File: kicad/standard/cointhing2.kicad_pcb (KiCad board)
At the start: 2 copper layers, 35 x 34 mm, 29 parts, among them J1 USB_B_Micro, Q1 BC847BS, Q2 S8050_J3Y, U1 CP2102-GMR_NRND, U2 ESP-12E, U3 AMS1117-3.3

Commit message: Update cointhing2.kicad_pcb
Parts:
- added QR*****: https://github.com/barn53/CoinThing/tree/2inch, https://github.com/barn53/CoinThing/tree/2inch, B.Cu at (170.8, 63.0)
- moved R6 26.6 mm to (174.9, 78.7)
- moved R7 26.6 mm to (174.9, 77.2)
- moved R1 26.1 mm to (149.3, 85.3), turned to 180 degrees
- moved R2 24.7 mm to (152.3, 85.3), turned to 180 degrees
- moved R4 22.3 mm to (152.3, 86.8), turned to 180 degrees
- moved Q1 21.7 mm to (174.9, 81.3)
- moved C7 6.89 mm to (177.0, 68.1), turned to 0 degrees
- moved C6 6.70 mm to (174.0, 68.1), turned to 180 degrees
- moved R11 3.88 mm to (169.1, 85.3), turned to 0 degrees
- moved R9 3.88 mm to (169.1, 86.8)
- moved REF** 3.70 mm to (171.4, 72.2)
- moved C8 2.78 mm to (166.1, 86.8)
- moved R10 2.78 mm to (166.1, 85.3), turned to 180 degrees
- moved C9 2.27 mm to (170.0, 62.2), turned to 90 degrees
- moved C5 0.61 mm to (160.7, 86.8)
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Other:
- outline, holes or cut-outs redrawn

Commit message: finished PCB rev.A
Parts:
- QR*****: footprint https://github.com/barn53/CoinThing/tree/2inch -> https:__github.com_barn53_CoinThing_tree_2inch
- renumbered REF** to h1, REF** to h2
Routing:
- net +3V3: track 0.00 -> 94.6 mm, vias 0 -> 5
- net VBUS: track 0.00 -> 42.9 mm
- net /GPIO0: track 0.00 -> 41.8 mm, vias 0 -> 2
- net Net-(R4-Pad2): track 0.00 -> 36.4 mm
- net /DTR: track 0.00 -> 32.1 mm
- net /TFT_BL: track 0.00 -> 31.4 mm, vias 0 -> 2
- net /~TFT_RES: track 0.00 -> 30.7 mm, vias 0 -> 2
- net /RTS: track 0.00 -> 30.5 mm, vias 0 -> 2
- net /~Reset: track 0.00 -> 26.5 mm, vias 0 -> 2
- net /D-: track 0.00 -> 16.9 mm, vias 0 -> 2
- net /D+: track 0.00 -> 16.8 mm, vias 0 -> 2
- net /VDD: track 0.00 -> 16.7 mm, vias 0 -> 2
- net Net-(R3-Pad2): track 0.00 -> 16.0 mm
- net /TFT_SDA: track 0.00 -> 12.5 mm, vias 0 -> 1
- net Net-(Q2-Pad1): track 0.00 -> 10.6 mm
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
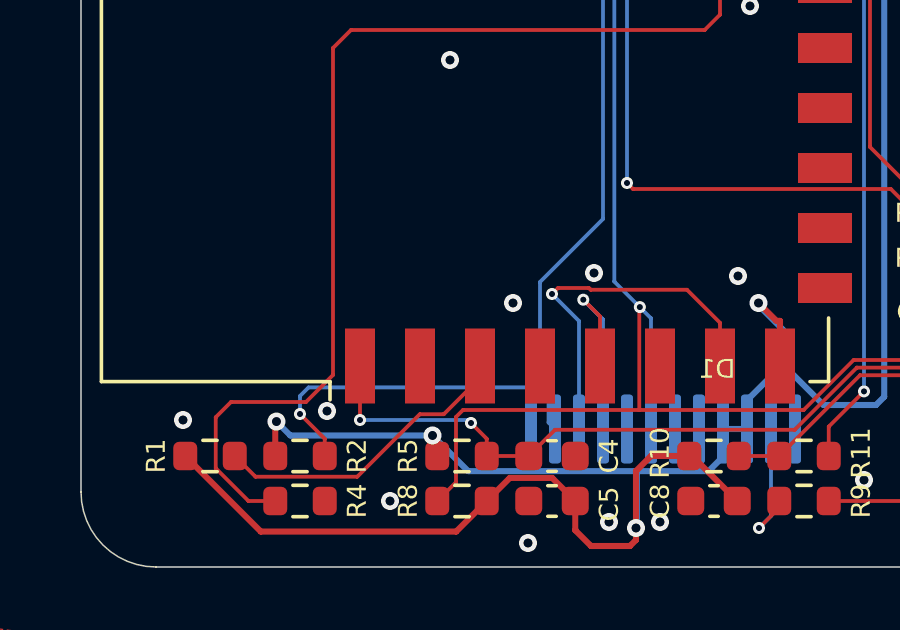
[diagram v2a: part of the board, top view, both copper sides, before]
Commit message: Wired deep sleep wakeup
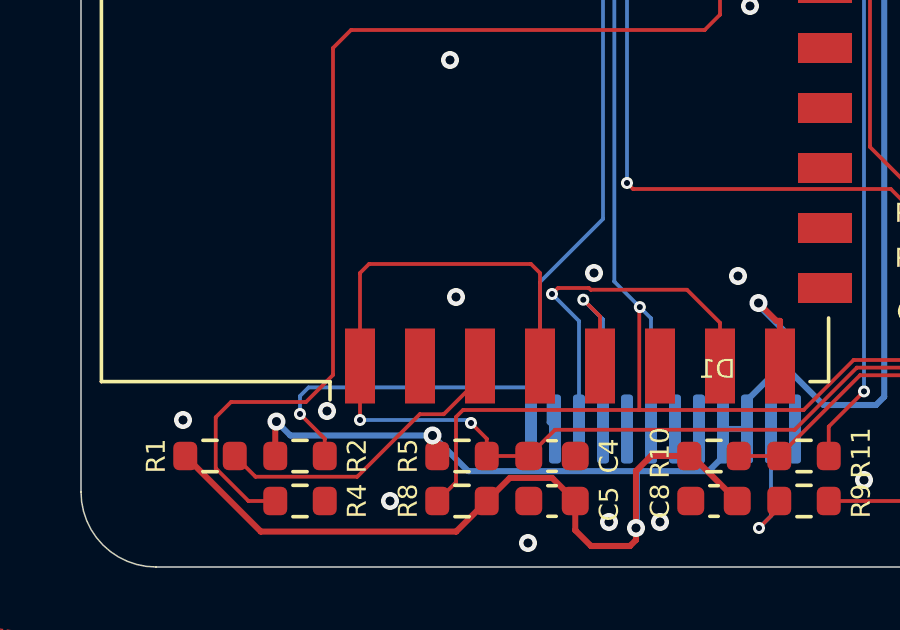
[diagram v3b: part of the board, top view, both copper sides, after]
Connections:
- J1 pad 4: (no net) -> Net-(J1-Pad4)
- U1 pad 1: (no net) -> Net-(U1-Pad1)
- U1 pad 10: (no net) -> Net-(U1-Pad10)
- U1 pad 11: (no net) -> Net-(U1-Pad11)
- U1 pad 12: (no net) -> Net-(U1-Pad12)
- U1 pad 13: (no net) -> Net-(U1-Pad13)
- U1 pad 14: (no net) -> Net-(U1-Pad14)
- U1 pad 15: (no net) -> Net-(U1-Pad15)
- U1 pad 16: (no net) -> Net-(U1-Pad16)
- U1 pad 17: (no net) -> Net-(U1-Pad17)
- U1 pad 18: (no net) -> Net-(U1-Pad18)
- U1 pad 19: (no net) -> Net-(U1-Pad19)
- U1 pad 2: (no net) -> Net-(U1-Pad2)
- U1 pad 20: (no net) -> Net-(U1-Pad20)
- U1 pad 21: (no net) -> Net-(U1-Pad21)
- U1 pad 22: (no net) -> Net-(U1-Pad22)
- U1 pad 23: (no net) -> Net-(U1-Pad23)
- U1 pad 27: (no net) -> Net-(U1-Pad27)
- U2 pad 10: (no net) -> Net-(U2-Pad10)
- U2 pad 11: (no net) -> Net-(U2-Pad11)
- U2 pad 12: (no net) -> Net-(U2-Pad12)
- U2 pad 13: (no net) -> Net-(U2-Pad13)
- U2 pad 14: (no net) -> Net-(U2-Pad14)
- U2 pad 2: (no net) -> Net-(U2-Pad2)
- U2 pad 20: (no net) -> /GPIO5
- U2 pad 4: (no net) -> /~Reset
- U2 pad 6: (no net) -> Net-(U2-Pad6)
- U2 pad 9: (no net) -> Net-(U2-Pad9)
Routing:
- net /~Reset: track 26.5 -> 39.0 mm
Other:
- board text added: "CoinThing 2" barn53 rev.B 01/22"
- board text removed: "CoinThing 2" barn53 rev.A 12/21"
